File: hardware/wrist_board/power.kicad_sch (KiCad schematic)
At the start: 15 parts, among them J1 S2B-PH-K-S_LF__SN_, P1 USB_C_Plug_USB2.0, U1 MCP73831T-2ACI_OT, U2 TLV75533PDBV

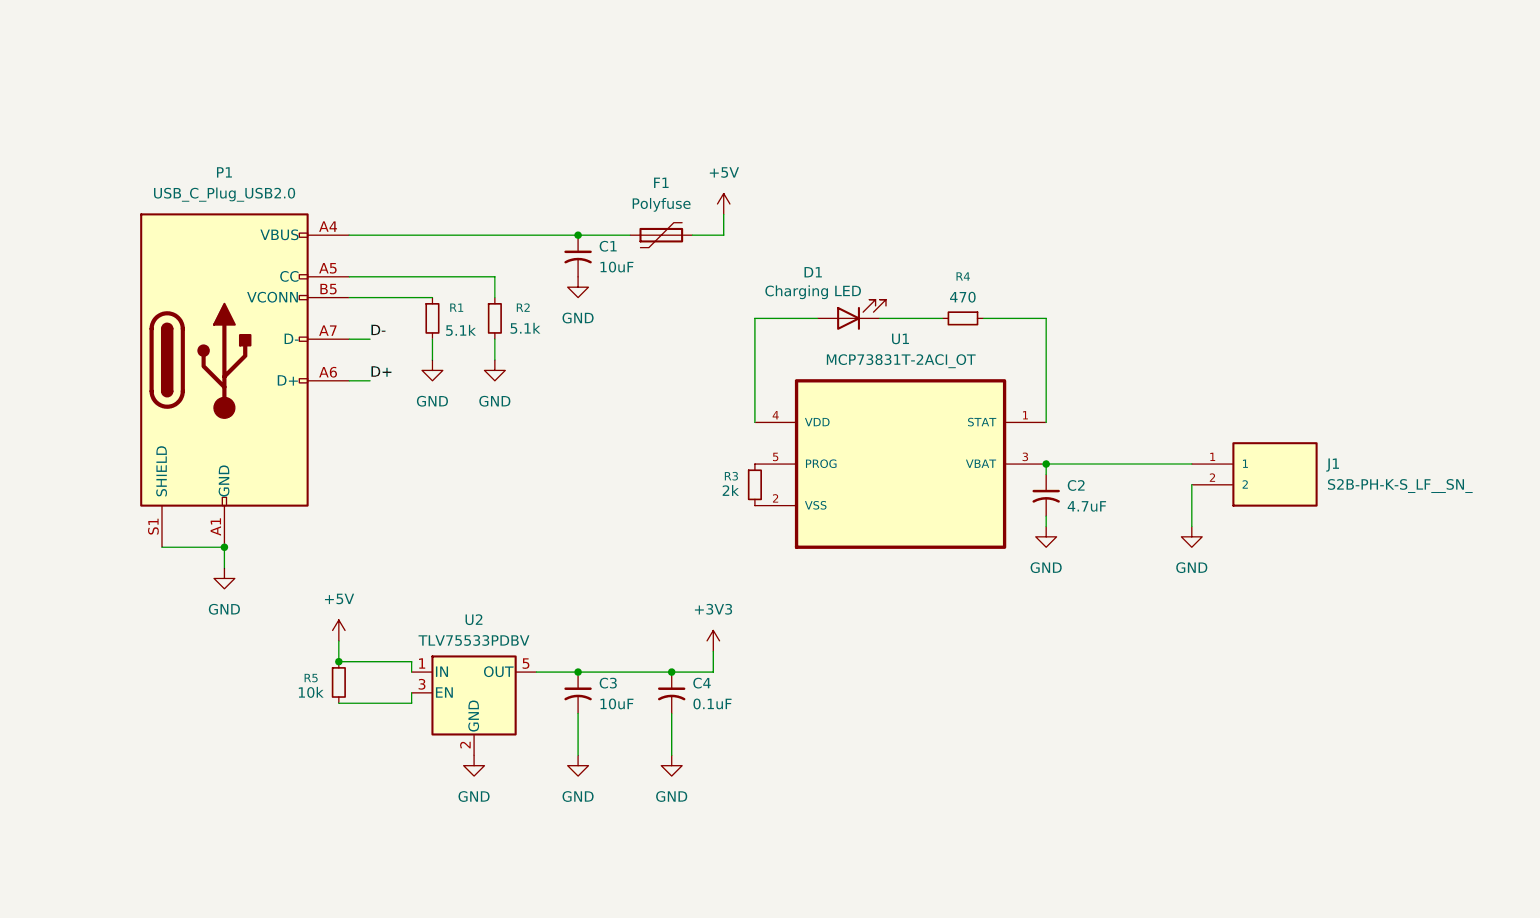
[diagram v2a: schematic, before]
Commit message: Added LEDs and power switch to power schematic
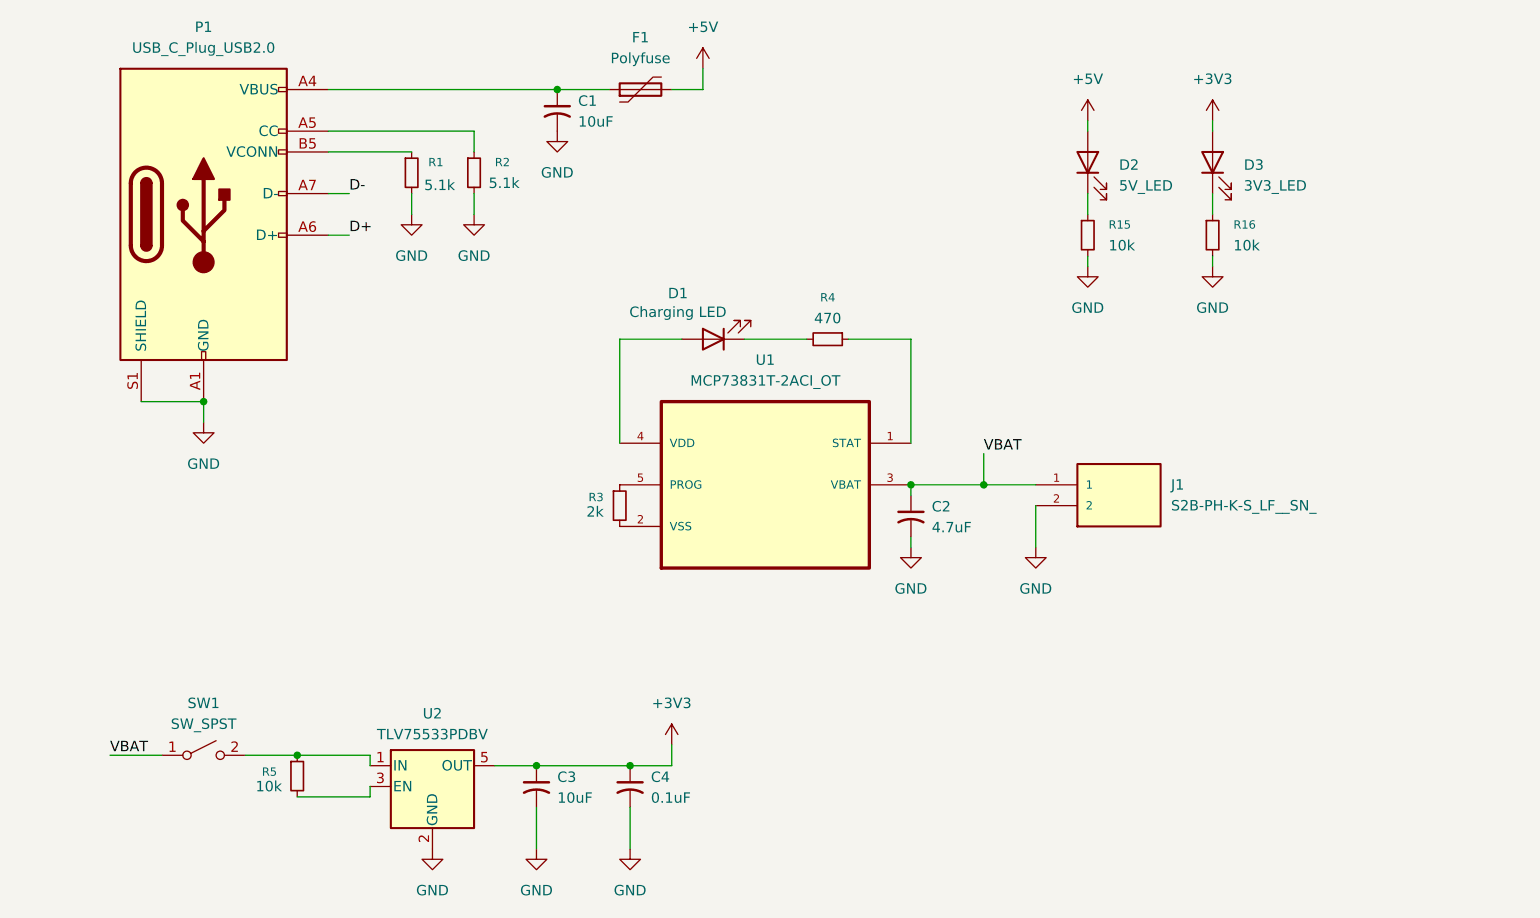
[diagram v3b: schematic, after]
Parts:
- added D2: 5V_LED, symbol Device:LED
- added D3: 3V3_LED, symbol Device:LED
- added R15, R16: 10k, symbol Device:R_Small
- added SW1: SW_SPST, symbol Switch:SW_SPST
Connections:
- net +3V3: now also D3.2 (A)
- net +5V: now also D2.2 (A); no longer R5.1, U2.1 (IN)
- net GND: now also R15.2, R16.2
- net at C2.1, J1.1, U1.3 (VBAT): now also SW1.1 (A)
- new net: D3.1 (K), R16.1
- new net: D2.1 (K), R15.1
- new net: R5.1, SW1.2 (B), U2.1 (IN)
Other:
- moved on the sheet: C1, C2, C3, C4, D1, F1, J1, P1, R1, R2, R3, R4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

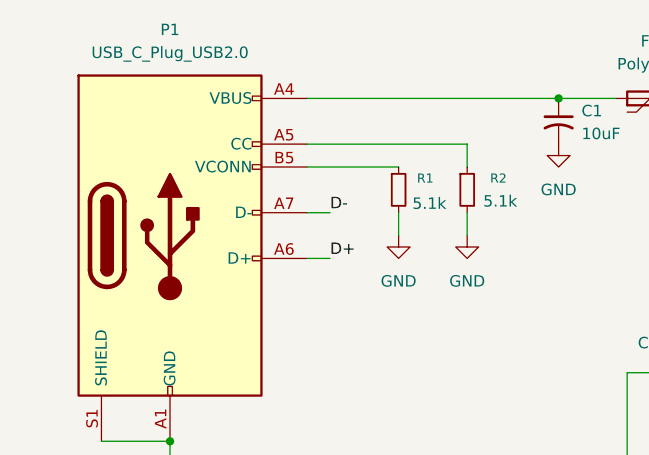
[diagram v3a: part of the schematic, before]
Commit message: USB C 2.0 receptacle updated
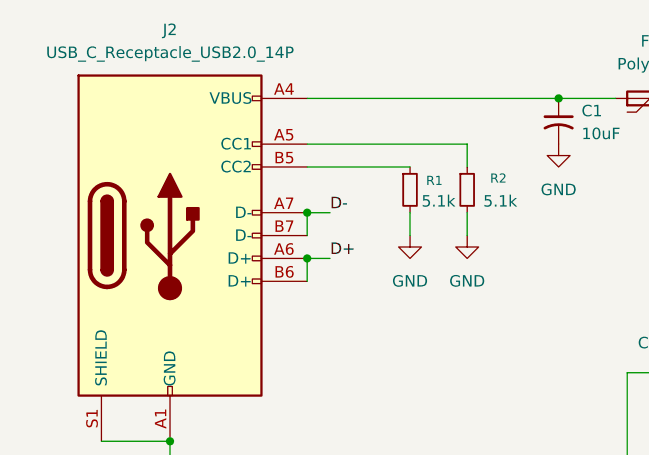
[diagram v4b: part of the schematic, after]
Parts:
- removed P1: USB_C_Plug_USB2.0, symbol Connector:USB_C_Plug_USB2.0
- added J2: USB_C_Receptacle_USB2.0_14P, symbol Connector:USB_C_Receptacle_USB2.0_14P
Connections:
- net D+: now also J2.A6 (D+), J2.B6 (D+)
- net D-: now also J2.A7 (D-), J2.B7 (D-)
- net GND: now also J2.A1 (GND), J2.A12 (GND), J2.B1 (GND), J2.B12 (GND), J2.S1 (SHIELD)
- net at C1.1, F1.1: now also J2.A4 (VBUS), J2.A9 (VBUS), J2.B4 (VBUS), J2.B9 (VBUS)
- net at R2.1: now also J2.A5 (CC1)
- net at R1.1: now also J2.B5 (CC2)

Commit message: Minor updates to both power and esp schematics
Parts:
- added C10: 0.1uF, symbol Device:C_Small_US
- R3: value 2k -> 10k
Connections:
- net +5V: now also D1.2 (A), U1.4 (VDD)
- net GND: now also R3.2, U1.2 (VSS), C10.2
- net at C2.1, J1.1, SW1.1 (A)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: now also C10.1
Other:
- moved on the sheet: J1, SW1

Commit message: All prototype footprints assigned
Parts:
- C1, C2, C3: footprint (none) -> Capacitor_SMD:C_0201_0603Metric
- C10, C4: footprint (none) -> Capacitor_SMD:C_0402_1005Metric
- D1, D2, D3: footprint (none) -> LED_SMD:LED_0201_0603Metric
- F1: footprint (none) -> Fuse:Fuse_0805_2012Metric
- J2: footprint (none) -> Connector_USB:USB_C_Receptacle_GCT_USB4105-xx-A_16P_TopMnt_Horizontal
- R1, R2, R5: footprint (none) -> Resistor_SMD:R_0402_1005Metric
- R15, R16, R4: footprint (none) -> Resistor_SMD:R_0603_1608Metric
- R3: footprint (none) -> LED_SMD:LED_0402_1005Metric
- SW1: footprint (none) -> Button_Switch_THT:SW_DIP_SPSTx01_Slide_6.7x4.1mm_W7.62mm_P2.54mm_LowProfile
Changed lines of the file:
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@@
 			)
 		)
-		(property "Footprint" ""
+		(property "Footprint" "Resistor_SMD:R_0603_1608Metric"
 			(at 208.28 77.47 0)
 			(effects
@@
 			)
 		)
-		(property "Footprint" ""
+		(property "Footprint" "LED_SMD:LED_0201_0603Metric"
 			(at 147.32 90.17 0)
 			(effects
@@
 			)
 		)
-		(property "Footprint" ""
+		(property "Footprint" "Fuse:Fuse_0805_2012Metric"
 			(at 143.51 58.42 0)
 			(effects
@@
 			)
 		)
-		(property "Footprint" ""
+		(property "Footprint" "Resistor_SMD:R_0603_1608Metric"
 			(at 193.04 77.47 0)
 			(effects
@@
 			)
 		)
-		(property "Footprint" ""
+		(property "Footprint" "Button_Switch_THT:SW_DIP_SPSTx01_Slide_6.7x4.1mm_W7.62mm_P2.54mm_LowProfile"
 			(at 73.66 140.97 0)
 			(effects
@@
 			)
 		)
-		(property "Footprint" ""
+		(property "Footprint" "Capacitor_SMD:C_0402_1005Metric"
 			(at 182.88 111.76 0)
 			(effects
@@
 			)
 		)
-		(property "Footprint" ""
+		(property "Footprint" "Capacitor_SMD:C_0201_0603Metric"
 			(at 125.73 144.78 0)
 			(effects
@@
 			)
 		)
-		(property "Footprint" ""
+		(property "Footprint" "LED_SMD:LED_0402_1005Metric"
 			(at 135.89 110.49 0)
 			(effects
@@
 			)
 		)
-		(property "Footprint" ""
+		(property "Footprint" "Resistor_SMD:R_0402_1005Metric"
 			(at 111.76 69.85 0)
 			(effects
@@
 			)
 		)
-		(property "Footprint" ""
+		(property "Footprint" "Connector_USB:USB_C_Receptacle_GCT_USB4105-xx-A_16P_TopMnt_Horizontal"
 			(at 88.9 74.93 0)
 			(effects
@@
 			)
 		)
-		(property "Footprint" ""
+		(property "Footprint" "LED_SMD:LED_0201_0603Metric"
 			(at 208.28 68.58 0)
 			(effects
@@
 			)
 		)
-		(property "Footprint" ""
+		(property "Footprint" "Resistor_SMD:R_0402_1005Metric"
 			(at 96.52 143.51 0)
 			(effects
@@
 			)
 		)
-		(property "Footprint" ""
+		(property "Footprint" "Capacitor_SMD:C_0402_1005Metric"
 			(at 137.16 144.78 0)
 			(effects
@@
 			)
 		)
-		(property "Footprint" ""
+		(property "Footprint" "Capacitor_SMD:C_0201_0603Metric"
 			(at 171.45 111.76 0)
 			(effects
@@
 			)
 		)
-		(property "Footprint" ""
+		(property "Footprint" "Resistor_SMD:R_0603_1608Metric"
 			(at 161.29 90.17 0)
 			(effects
@@
 			)
 		)
-		(property "Footprint" ""
+		(property "Footprint" "Capacitor_SMD:C_0201_0603Metric"
 			(at 128.27 62.23 0)
 			(effects
@@
 			)
 		)
-		(property "Footprint" ""
+		(property "Footprint" "LED_SMD:LED_0201_0603Metric"
 			(at 193.04 68.58 0)
 			(effects
@@
 			)
 		)
-		(property "Footprint" ""
+		(property "Footprint" "Resistor_SMD:R_0402_1005Metric"
 			(at 118.11 69.85 0)
 			(effects

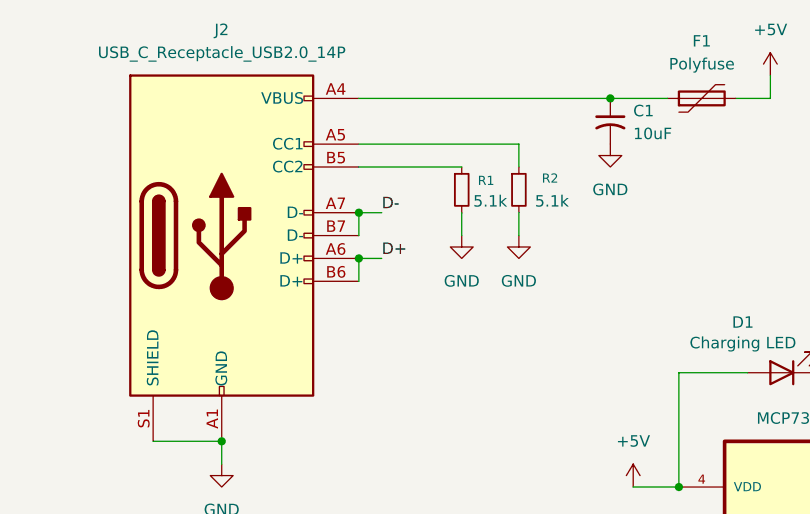
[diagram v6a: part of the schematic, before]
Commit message: Schematics condensed into one, labels added
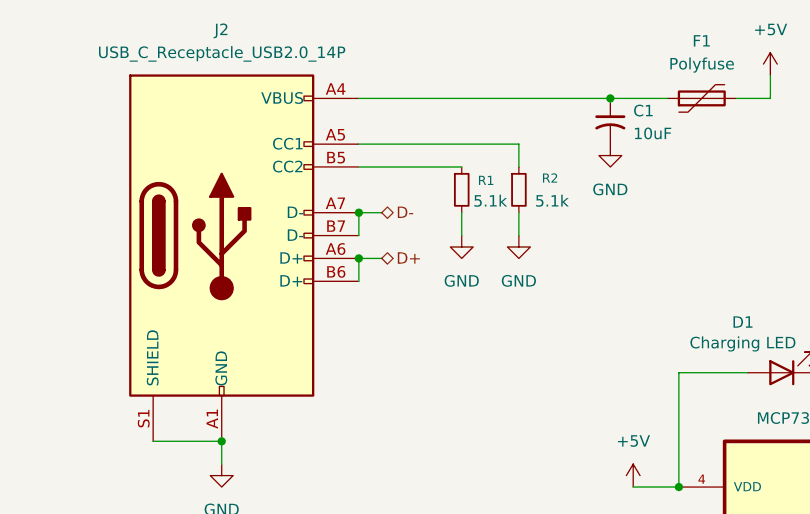
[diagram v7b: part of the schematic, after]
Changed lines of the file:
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@@
-		)
-	)
-	(label "D-"
-		(at 102.87 72.39 0)
-		(effects
-			(font
-				(size 1.27 1.27)
-			)
-			(justify left bottom)
 		)
 	)
@@
 		)
 	)
-	(label "D+"
+	(hierarchical_label "D+"
+		(shape bidirectional)
 		(at 102.87 77.47 0)
 		(effects
@@
 				(size 1.27 1.27)
 			)
-			(justify left bottom)
+			(justify left)
 		)
 	)
+	(hierarchical_label "D-"
+		(shape bidirectional)
+		(at 102.87 72.39 0)
+		(effects
+			(font
+				(size 1.27 1.27)
+			)
+			(justify left)
+		)
+	)
